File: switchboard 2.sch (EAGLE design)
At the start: 230 parts, among them IC1 MT8816AP, IC10 Z8F2480SO, IC11 LMV321M5, IC12 74HC595D, IC14 74LVC1G125DBV, IC15 74LVC1G125DBV, IC16 LM2940-9, IC17 PC817S OPTO, IC2 NE5532D, IC3 TC7660-SOIC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

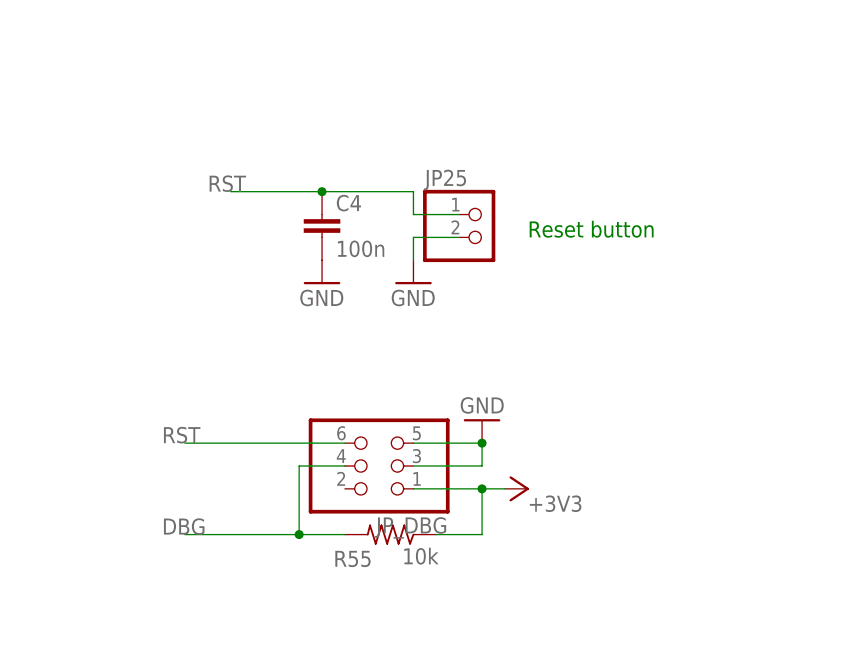
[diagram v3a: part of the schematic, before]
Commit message: Layout changes to improve manufacturability and EMC. RESET pin removed.
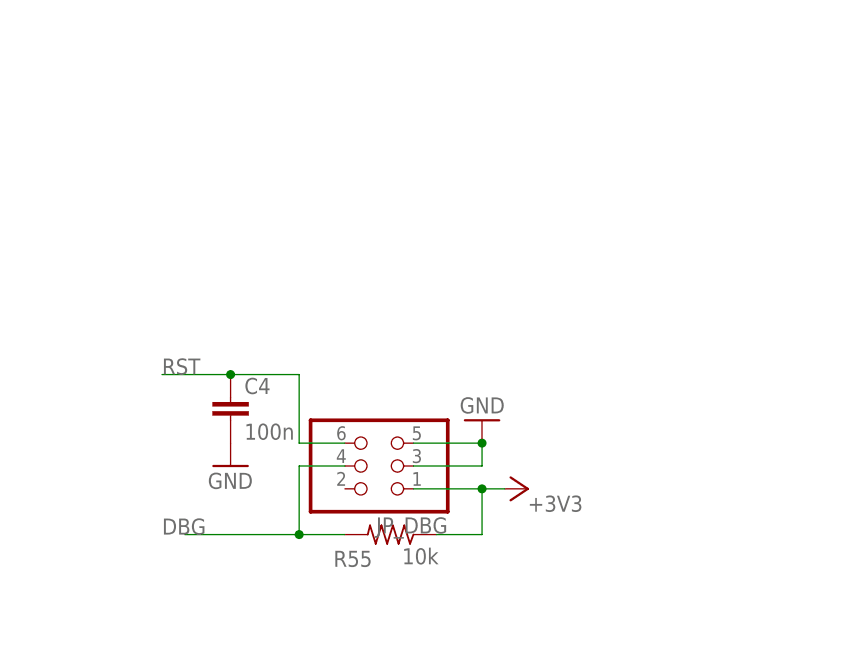
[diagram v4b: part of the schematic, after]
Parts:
- removed JP25: (no value), pinhead:PINHD-1X2
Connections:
- net GND: no longer JP25.2
- net RST: no longer JP25.1
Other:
- note removed: "Reset button"
- moved on the sheet: C4
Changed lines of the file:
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@@
 <part name="C4" library="rcl" deviceset="C-EU" device="C0603" value="100n"/>
 <part name="GND4" library="supply1" deviceset="GND" device=""/>
-<part name="JP25" library="pinhead" deviceset="PINHD-1X2" device=""/>
-<part name="GND39" library="supply1" deviceset="GND" device=""/>
 <part name="R60" library="rcl" deviceset="R-US_" device="R0603" value="1k SMD"/>
 <part name="R71" library="rcl" deviceset="R-US_" device="R0603" value="1k"/>
@@
 2-3 - MIDI Out</text>
 <text x="-106.68" y="-325.12" size="1.778" layer="97">The DC blocking caps are optional and may be changed to 0R jumpers if it is guaranteed that the effects inputs and outputs doesn't have DC voltages.</text>
-<text x="203.2" y="66.04" size="1.778" layer="91">Reset button</text>
 <text x="-279.4" y="99.06" size="1.778" layer="97">TX/RX LED</text>
 <text x="-154.94" y="58.42" size="1.778" layer="97">Buttons</text>
@@
 <attribute name="VALUE" x="203.2" y="35.56" size="1.778" layer="96"/>
 </instance>
-<instance part="C4" gate="G$1" x="180.34" y="68.58"/>
-<instance part="GND4" gate="1" x="180.34" y="60.96"/>
-<instance part="JP25" gate="G$1" x="198.12" y="66.04"/>
-<instance part="GND39" gate="1" x="190.5" y="60.96"/>
+<instance part="C4" gate="G$1" x="170.18" y="48.26"/>
+<instance part="GND4" gate="1" x="170.18" y="40.64"/>
 <instance part="R60" gate="G$1" x="-330.2" y="233.68" smashed="yes">
 <attribute name="NAME" x="-328.93" y="237.2614" size="1.778" layer="95" rot="R180"/>
@@
 </segment>
 <segment>
-<pinref part="JP25" gate="G$1" pin="2"/>
-<wire x1="195.58" y1="66.04" x2="190.5" y2="66.04" width="0.1524" layer="91"/>
-<wire x1="190.5" y1="66.04" x2="190.5" y2="63.5" width="0.1524" layer="91"/>
-<pinref part="GND39" gate="1" pin="GND"/>
-</segment>
-<segment>
 <pinref part="GND80" gate="1" pin="GND"/>
 <pinref part="GAP1" gate="G$1" pin="2"/>
@@
 <segment>
 <pinref part="JP_DBG" gate="A" pin="6"/>
-<wire x1="182.88" y1="43.18" x2="165.1" y2="43.18" width="0.1524" layer="91"/>
-<label x="162.56" y="43.18" size="1.778" layer="95"/>
+<wire x1="182.88" y1="43.18" x2="177.8" y2="43.18" width="0.1524" layer="91"/>
+<label x="162.56" y="50.8" size="1.778" layer="95"/>
+<wire x1="177.8" y1="43.18" x2="177.8" y2="50.8" width="0.1524" layer="91"/>
+<wire x1="177.8" y1="50.8" x2="170.18" y2="50.8" width="0.1524" layer="91"/>
+<pinref part="C4" gate="G$1" pin="1"/>
+<wire x1="170.18" y1="50.8" x2="162.56" y2="50.8" width="0.1524" layer="91"/>
+<junction x="170.18" y="50.8"/>
 </segment>
 <segment>
@@
 <pinref part="IC10" gate="G$1" pin="!RESET!/PD0"/>
 </segment>
-<segment>
-<pinref part="C4" gate="G$1" pin="1"/>
-<wire x1="180.34" y1="71.12" x2="190.5" y2="71.12" width="0.1524" layer="91"/>
-<wire x1="190.5" y1="71.12" x2="190.5" y2="68.58" width="0.1524" layer="91"/>
-<pinref part="JP25" gate="G$1" pin="1"/>
-<wire x1="190.5" y1="68.58" x2="195.58" y2="68.58" width="0.1524" layer="91"/>
-<wire x1="180.34" y1="71.12" x2="170.18" y2="71.12" width="0.1524" layer="91"/>
-<junction x="180.34" y="71.12"/>
-<label x="167.64" y="71.12" size="1.778" layer="95"/>
-</segment>
 </net>

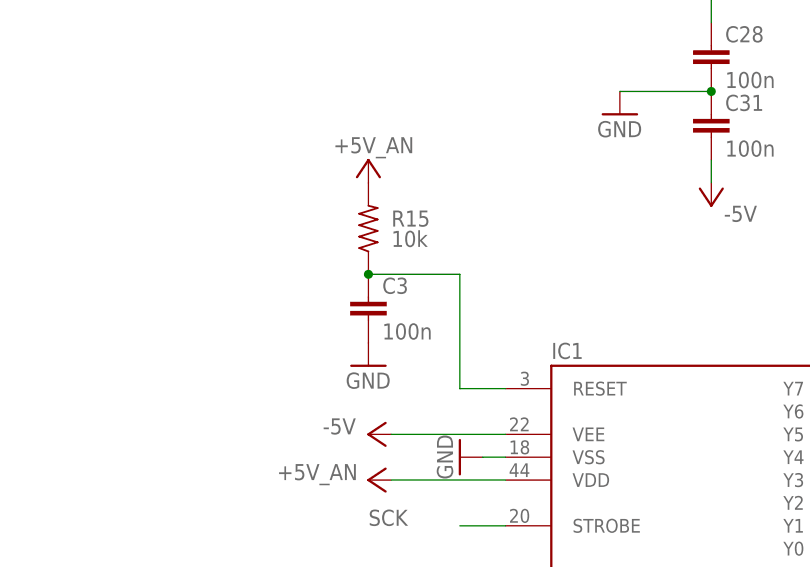
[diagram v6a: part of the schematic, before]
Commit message: PCB version 1 fixes
- Crosspoint switch MT8816 reset pin is active high. Resistor and capacitor positions on schematic and layout switched accordingly.
- Audio out 1 and 2 silkscreen position corrected.
- Resistors values on IC9 feedback paths changed from 1 M to undefined (to be defined if needed).
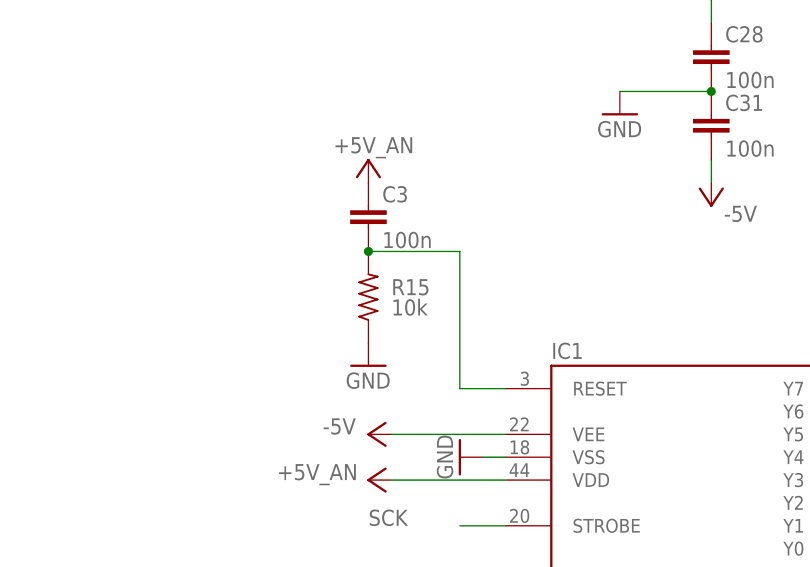
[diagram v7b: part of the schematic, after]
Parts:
- R39, R41, R42, R43: value 1M SMD -> X
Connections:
- removed net N$11: C3.1, IC1.RESET, R15.1
- new net N$84: C3.2, IC1.RESET, R15.2
- net +5V_AN: now also C3.1; no longer R15.2
- net GND: now also R15.1; no longer C3.2
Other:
- moved on the sheet: C3, R15
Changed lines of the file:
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@@
 <?xml version="1.0" encoding="utf-8"?>
 <!DOCTYPE eagle SYSTEM "eagle.dtd">
-<eagle version="8.3.2">
+<eagle version="9.1.3">
 <drawing>
 <settings>
@@
 <part name="GND49" library="supply1" deviceset="GND" device=""/>
 <part name="IC17" library="PATSKO" deviceset="OPTOCOUPLER" device="" value="PC817S OPTO"/>
-<part name="R39" library="rcl" deviceset="R-US_" device="R0603" value="1M SMD"/>
+<part name="R39" library="rcl" deviceset="R-US_" device="R0603" value="X"/>
 <part name="GND61" library="supply1" deviceset="GND" device=""/>
-<part name="R41" library="rcl" deviceset="R-US_" device="R0603" value="1M SMD"/>
-<part name="R42" library="rcl" deviceset="R-US_" device="R0603" value="1M SMD"/>
-<part name="R43" library="rcl" deviceset="R-US_" device="R0603" value="1M SMD"/>
+<part name="R41" library="rcl" deviceset="R-US_" device="R0603" value="X"/>
+<part name="R42" library="rcl" deviceset="R-US_" device="R0603" value="X"/>
+<part name="R43" library="rcl" deviceset="R-US_" device="R0603" value="X"/>
 <part name="GND93" library="supply1" deviceset="GND" device=""/>
 <part name="SJ2" library="jumper" deviceset="SJ" device=""/>
@@
 </instance>
 <instance part="GND8" gate="1" x="355.6" y="-167.64" rot="R270"/>
-<instance part="C3" gate="G$1" x="345.44" y="-149.86"/>
+<instance part="C3" gate="G$1" x="345.44" y="-139.7"/>
 <instance part="GND15" gate="1" x="345.44" y="-157.48"/>
-<instance part="R15" gate="G$1" x="345.44" y="-142.24" smashed="yes" rot="R90">
-<attribute name="NAME" x="347.98" y="-142.0114" size="1.778" layer="95"/>
-<attribute name="VALUE" x="347.98" y="-144.272" size="1.778" layer="96"/>
+<instance part="R15" gate="G$1" x="345.44" y="-149.86" smashed="yes" rot="R90">
+<attribute name="NAME" x="347.98" y="-149.6314" size="1.778" layer="95"/>
+<attribute name="VALUE" x="347.98" y="-151.892" size="1.778" layer="96"/>
 </instance>
 <instance part="IC2" gate="A" x="40.64" y="-231.14"/>
@@
 </segment>
 <segment>
-<pinref part="C3" gate="G$1" pin="2"/>
-<pinref part="GND15" gate="1" pin="GND"/>
-</segment>
-<segment>
 <pinref part="R14" gate="G$1" pin="1"/>
 <pinref part="GND16" gate="1" pin="GND"/>
@@
 <pinref part="GND106" gate="1" pin="GND"/>
 </segment>
+<segment>
+<pinref part="GND15" gate="1" pin="GND"/>
+<pinref part="R15" gate="G$1" pin="1"/>
+</segment>
 </net>
 <net name="SW_IN_1" class="0">
@@
 </segment>
 </net>
-<net name="N$11" class="0">
-<segment>
-<pinref part="C3" gate="G$1" pin="1"/>
-<wire x1="345.44" y1="-147.32" x2="355.6" y2="-147.32" width="0.1524" layer="91"/>
-<wire x1="355.6" y1="-147.32" x2="355.6" y2="-160.02" width="0.1524" layer="91"/>
-<pinref part="IC1" gate="G$1" pin="RESET"/>
-<wire x1="355.6" y1="-160.02" x2="360.68" y2="-160.02" width="0.1524" layer="91"/>
-<pinref part="R15" gate="G$1" pin="1"/>
-<junction x="345.44" y="-147.32"/>
-</segment>
-</net>
 <net name="SWOUT_2-TO_EFF_7" class="0">
 <segment>
@@
 </segment>
 <segment>
-<pinref part="R15" gate="G$1" pin="2"/>
-<pinref part="P+22" gate="1" pin="+5V_AN"/>
-</segment>
-<segment>
 <pinref part="D2" gate="G$1" pin="C"/>
 <wire x1="-15.24" y1="-121.92" x2="-15.24" y2="-119.38" width="0.1524" layer="91"/>
@@
 <wire x1="147.32" y1="-124.46" x2="147.32" y2="-127" width="0.1524" layer="91"/>
 </segment>
+<segment>
+<pinref part="P+22" gate="1" pin="+5V_AN"/>
+<pinref part="C3" gate="G$1" pin="1"/>
+</segment>
 </net>
 <net name="+9V" class="0">
@@
 </segment>
 </net>
+<net name="N$84" class="0">
+<segment>
+<pinref part="C3" gate="G$1" pin="2"/>
+<pinref part="R15" gate="G$1" pin="2"/>
+<wire x1="355.6" y1="-144.78" x2="355.6" y2="-160.02" width="0.1524" layer="91"/>
+<pinref part="IC1" gate="G$1" pin="RESET"/>
+<wire x1="355.6" y1="-160.02" x2="360.68" y2="-160.02" width="0.1524" layer="91"/>
+<wire x1="345.44" y1="-144.78" x2="355.6" y2="-144.78" width="0.1524" layer="91"/>
+<junction x="345.44" y="-144.78"/>
+</segment>
+</net>
